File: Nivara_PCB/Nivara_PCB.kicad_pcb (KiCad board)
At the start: 2 copper layers, 102.2 x 83 mm, 40 parts, among them J1 NPN_IN, J10 PNP_OUT, J11 Analog_Out, J2 PNP_IN, J3 D_IN, J4 NPN_OUT, J5 RELAY, J6 RUN/STOP, J7 FUENTE, J8 RS485, J9 Analaog_In, Q1 IRLML6344, Q2 IRLML6344, U1 ESP32-S3-WROOM-1, U2 AP63203WU, U4 AP63205WU

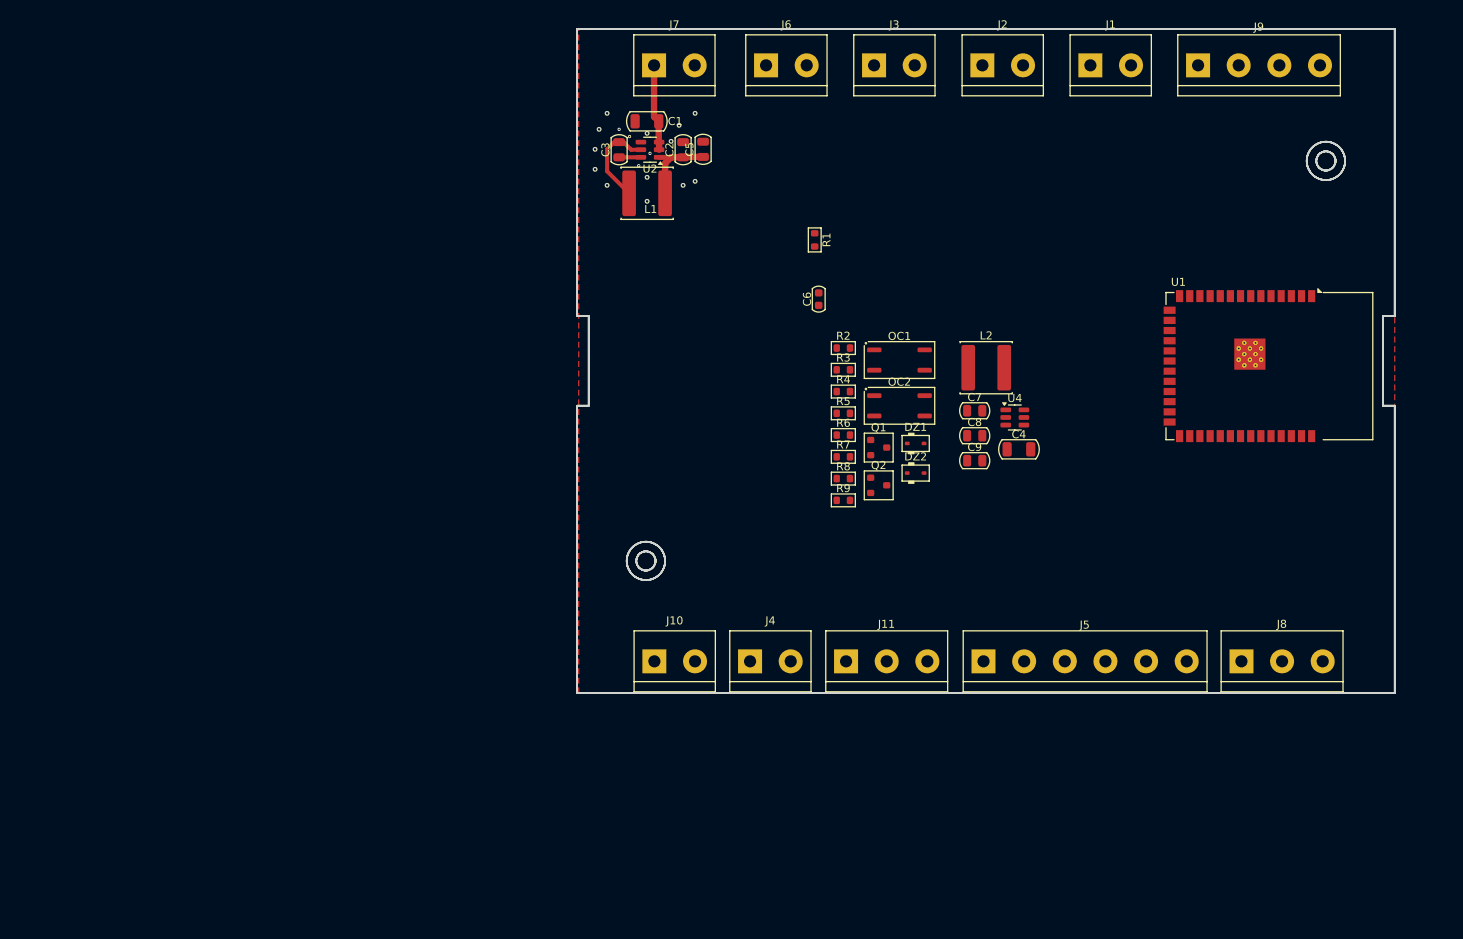
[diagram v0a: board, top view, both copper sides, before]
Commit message: Añadido de funciones NPN/PNP
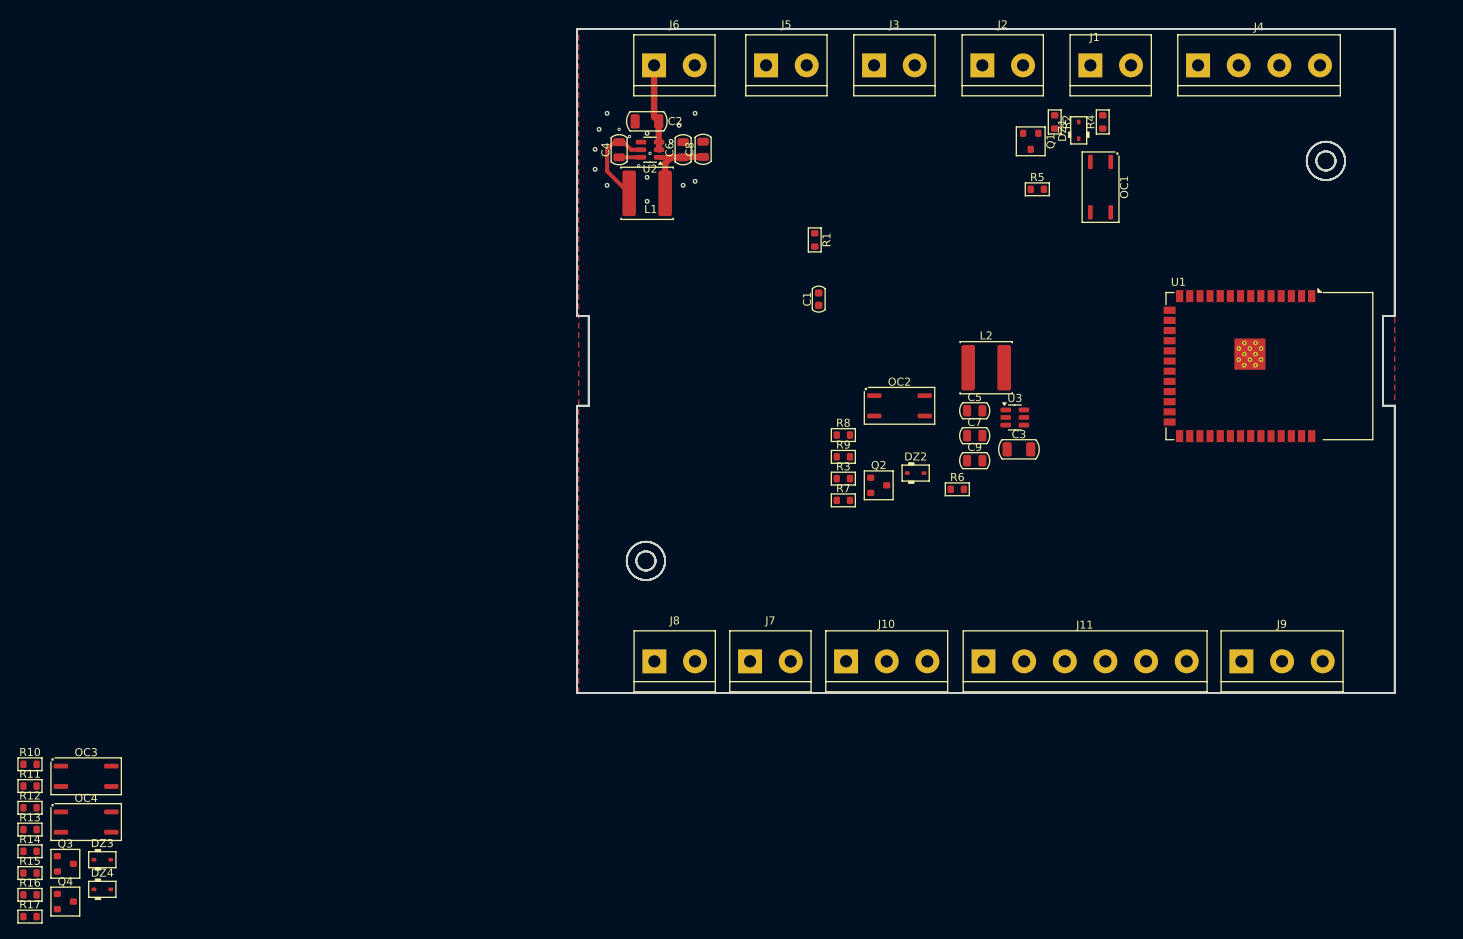
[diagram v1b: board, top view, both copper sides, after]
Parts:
- added DZ3: BZT52C10S, PCM_Diode_SMD_AKL:D_SOD-323, F.Cu at (39.0, 148.8)
- added DZ4: BZT52C10S, PCM_Diode_SMD_AKL:D_SOD-323, F.Cu at (39.0, 152.5)
- added OC3: LTV-356T, PCM_Package_SO_AKL:SO-4_4.4x3.9mm_P2.54mm, F.Cu at (36.9, 138.4)
- added OC4: LTV-356T, PCM_Package_SO_AKL:SO-4_4.4x3.9mm_P2.54mm, F.Cu at (36.9, 144.1)
- added Q3: IRLML6402, PCM_Package_TO_SOT_SMD_AKL:SOT-23, F.Cu at (34.3, 149.3)
- added Q4: IRLML6402, PCM_Package_TO_SOT_SMD_AKL:SOT-23, F.Cu at (34.3, 154.0)
- added R10: 7k, PCM_Resistor_SMD_AKL:R_0603_1608Metric, F.Cu at (29.9, 136.9)
- added R11: 22k, PCM_Resistor_SMD_AKL:R_0603_1608Metric, F.Cu at (29.9, 139.6)
- added R12: 1k, PCM_Resistor_SMD_AKL:R_0603_1608Metric, F.Cu at (29.9, 142.3)
- added R13: 10k, PCM_Resistor_SMD_AKL:R_0603_1608Metric, F.Cu at (29.9, 145.0)
- added R14: 7k, PCM_Resistor_SMD_AKL:R_0603_1608Metric, F.Cu at (29.9, 147.8)
- added R15: 22k, PCM_Resistor_SMD_AKL:R_0603_1608Metric, F.Cu at (29.9, 150.5)
- added R16: 1k, PCM_Resistor_SMD_AKL:R_0603_1608Metric, F.Cu at (29.9, 153.2)
- added R17: 10k, PCM_Resistor_SMD_AKL:R_0603_1608Metric, F.Cu at (29.9, 155.9)
- moved R4 46.8 mm to (164.0, 56.6), turned to 90 degrees
- moved DZ1 44.1 mm to (161.0, 57.6), turned to 90 degrees
- moved Q1 42.7 mm to (155.0, 59.0), turned to -90 degrees
- moved R2 38.7 mm to (158.0, 56.6), turned to -90 degrees
- moved R5 37.0 mm to (155.8, 65.0)
- moved OC1 33.1 mm to (163.7, 64.7), turned to -90 degrees
- moved R6 20.6 mm to (145.8, 102.5)
- renumbered C6 to C1, C1 to C2, C4 to C3, C3 to C4, C7 to C5, C2 to C6, C8 to C7, C5 to C8, J11 to J10, J5 to J11, J9 to J4, J6 to J5, J7 to J6, J4 to J7, J10 to J8, J8 to J9, R8 to R3, R3 to R6, R9 to R7, R6 to R8, R7 to R9, U4 to U3

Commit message: Cambios en pcb
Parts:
- moved R7 58.4 mm to (169.0, 59.0)
- moved Q2 58.4 mm to (172.0, 56.0)
- moved DZ2 52.4 mm to (168.0, 55.8), turned to 90 degrees
- moved R8 50.4 mm to (169.0, 62.0), turned to 90 degrees
- moved R6 50.3 mm to (165.0, 56.0), turned to -90 degrees
- moved R9 49.5 mm to (169.0, 66.0), turned to -90 degrees
- moved R3 48.0 mm to (156.0, 59.8), turned to -90 degrees
- moved OC2 45.0 mm to (173.0, 63.0), turned to -90 degrees
- moved R4 8.03 mm to (159.2, 63.0), turned to 0 degrees
- moved Q1 5.10 mm to (160.0, 60.0), turned to 0 degrees
- moved R5 3.50 mm to (159.2, 66.0)
- moved OC1 1.87 mm to (164.7, 63.1)
- moved DZ1 1.63 mm to (161.0, 56.0)
- moved R2 0.75 mm to (158.0, 55.8)

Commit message: Cambios en archivos a subir
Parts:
- added TP1: +VCC, TestPoint:TestPoint_Pad_1.0x1.0mm, F.Cu at (103.7, 55.1)
- added TP2: +3.3V, TestPoint:TestPoint_Pad_1.0x1.0mm, F.Cu at (105.9, 72.1)
- added TP3: +5V, TestPoint:TestPoint_Pad_1.0x1.0mm, F.Cu at (118.5, 58.4)
- added TP4: GND, TestPoint:TestPoint_Pad_1.0x1.0mm, F.Cu at (103.4, 51.7)
- moved C1 60.0 mm to (188.4, 75.2), turned to 180 degrees
- moved C3 59.1 mm to (109.9, 57.6)
- moved R1 56.5 mm to (184.4, 75.6), turned to 0 degrees
- moved U3 53.4 mm to (110.6, 61.1), turned to -90 degrees
- moved C9 53.1 mm to (113.5, 58.6), turned to 90 degrees
- moved C7 49.1 mm to (115.9, 58.6), turned to 90 degrees
- moved C5 42.3 mm to (112.9, 69.2)
- moved L2 40.9 mm to (116.0, 63.7)
- moved C8 8.31 mm to (108.2, 65.9), turned to -90 degrees
- moved C6 6.03 mm to (110.6, 66.0), turned to -90 degrees
- moved L1 3.76 mm to (103.8, 67.4)
- moved C2 3.28 mm to (104.9, 59.0)
- moved C4 2.43 mm to (102.1, 62.0)
- moved U2 2.43 mm to (106.0, 62.0)
- moved Q2 1.17 mm to (172.6, 57.0)
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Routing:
- net +5V: track 0.00 -> 26.5 mm
- net +3.3V: track 11.8 -> 26.7 mm
- net VCC: track 10.8 -> 23.5 mm
- net Net-(U3-SW): track 0.00 -> 10.8 mm
- net Net-(DZ2-K): track 0.00 -> 9.40 mm
- net Net-(DZ1-K): track 0.00 -> 8.39 mm
- net /NIVARA_BOARD/NPN_IN_1: track 0.00 -> 8.27 mm
- net /NIVARA_BOARD/NPN_IN/ESP_NPN_IN_1: track 0.00 -> 7.84 mm
- net /NIVARA_BOARD/NPN_IN_2: track 0.00 -> 7.65 mm
- net Net-(OC1-Pad1): track 0.00 -> 7.24 mm
- net Net-(U3-BST): track 0.00 -> 7.07 mm
- net /NIVARA_BOARD/NPN_IN/ESP_NPN_IN_2: track 0.00 -> 6.85 mm
- net Net-(OC2-Pad1): track 0.00 -> 5.84 mm
- net Net-(Q2-D): track 0.00 -> 4.55 mm
- net Net-(Q1-D): track 0.00 -> 2.46 mm
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- added copper zone on B.Cu, net GND

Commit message: Cambios en el diseño del pcb
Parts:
- moved R16 159.2 mm to (157.7, 58.3), turned to 180 degrees
- moved R15 158.8 mm to (157.2, 55.5), turned to -90 degrees
- moved R17 156.4 mm to (157.5, 65.4), turned to 90 degrees
- moved Q4 154.5 mm to (158.2, 61.6), turned to -90 degrees
- moved R14 153.7 mm to (152.8, 55.4), turned to -90 degrees
- moved DZ4 151.4 mm to (155.2, 55.5), turned to -90 degrees
- moved R10 144.5 mm to (149.3, 55.5), turned to -90 degrees
- moved OC4 142.5 mm to (153.5, 62.2), turned to -90 degrees
- moved DZ3 142.5 mm to (146.6, 55.5), turned to -90 degrees
- moved R11 141.8 mm to (144.0, 55.4), turned to -90 degrees
- moved R12 141.4 mm to (143.7, 58.4)
- moved Q3 139.9 mm to (143.5, 61.8)
- moved R13 139.1 mm to (143.8, 65.2)
- moved OC3 134.8 mm to (148.1, 62.1), turned to -90 degrees
- moved R5 10.4 mm to (169.2, 70.2), turned to -90 degrees
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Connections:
- R14 pad 1: /NIVARA_BOARD/PNP_IN_1 -> /NIVARA_BOARD/PNP_IN_2
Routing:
- net Net-(DZ3-K): track 0.00 -> 13.8 mm
- net Net-(DZ4-K): track 0.00 -> 12.3 mm
- net +3.3V: track 26.7 -> 16.5 mm
- net /NIVARA_BOARD/NPN_IN/ESP_NPN_IN_1: track 7.84 -> 0.00 mm
- net /NIVARA_BOARD/PNP_IN/ESP_PNP_IN_1: track 0.00 -> 6.69 mm
- net Net-(Q3-D): track 0.00 -> 6.05 mm
- net /NIVARA_BOARD/PNP_IN_2: track 0.00 -> 5.59 mm
- net /NIVARA_BOARD/PNP_IN_1: track 0.00 -> 5.29 mm
- net Net-(Q3-S): track 0.00 -> 5.19 mm
- net Net-(Q4-D): track 0.00 -> 5.18 mm
- net /NIVARA_BOARD/PNP_IN/ESP_PNP_IN_2: track 0.00 -> 3.05 mm
- net Net-(Q4-S): track 0.00 -> 2.42 mm
- net Net-(Q1-D): track 2.46 -> 4.35 mm
- net +5V: track 26.5 -> 24.7 mm
- net Net-(DZ1-K): track 8.39 -> 6.96 mm
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
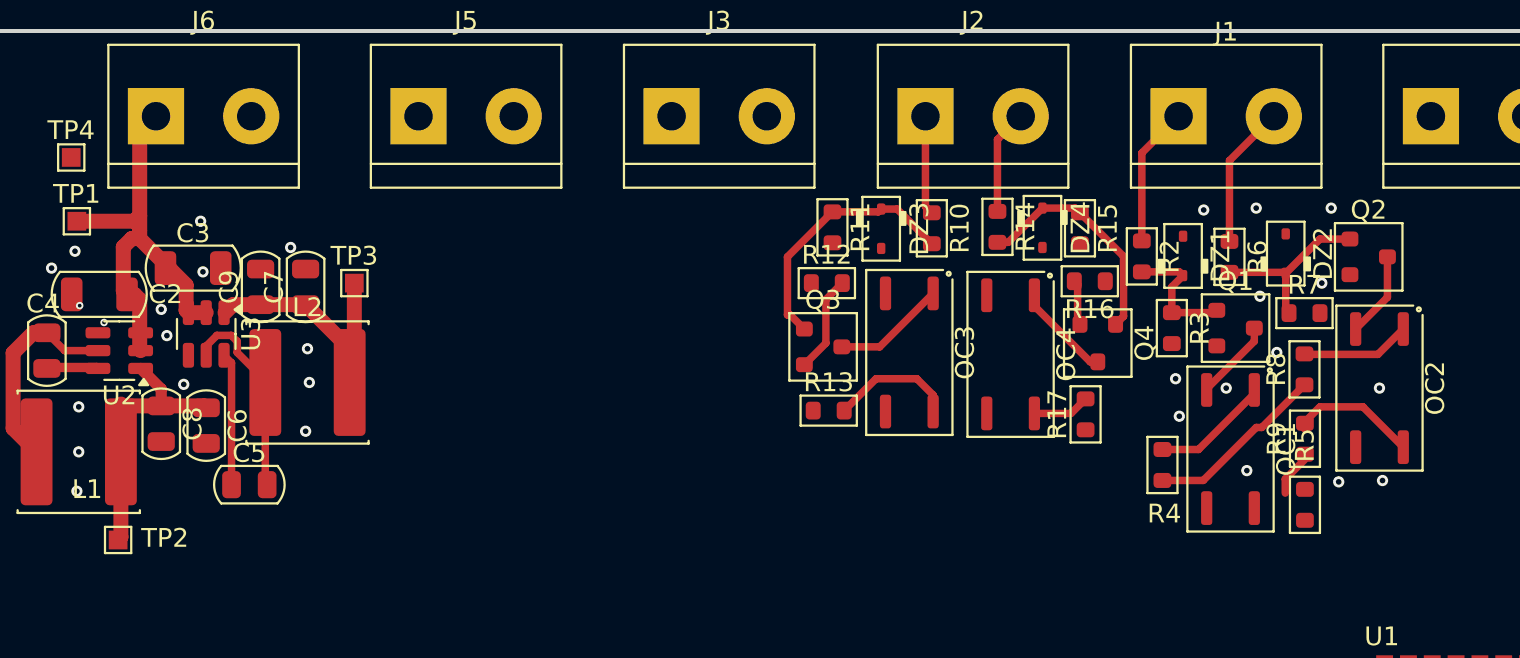
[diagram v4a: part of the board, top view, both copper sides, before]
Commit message: Modificación del PCB
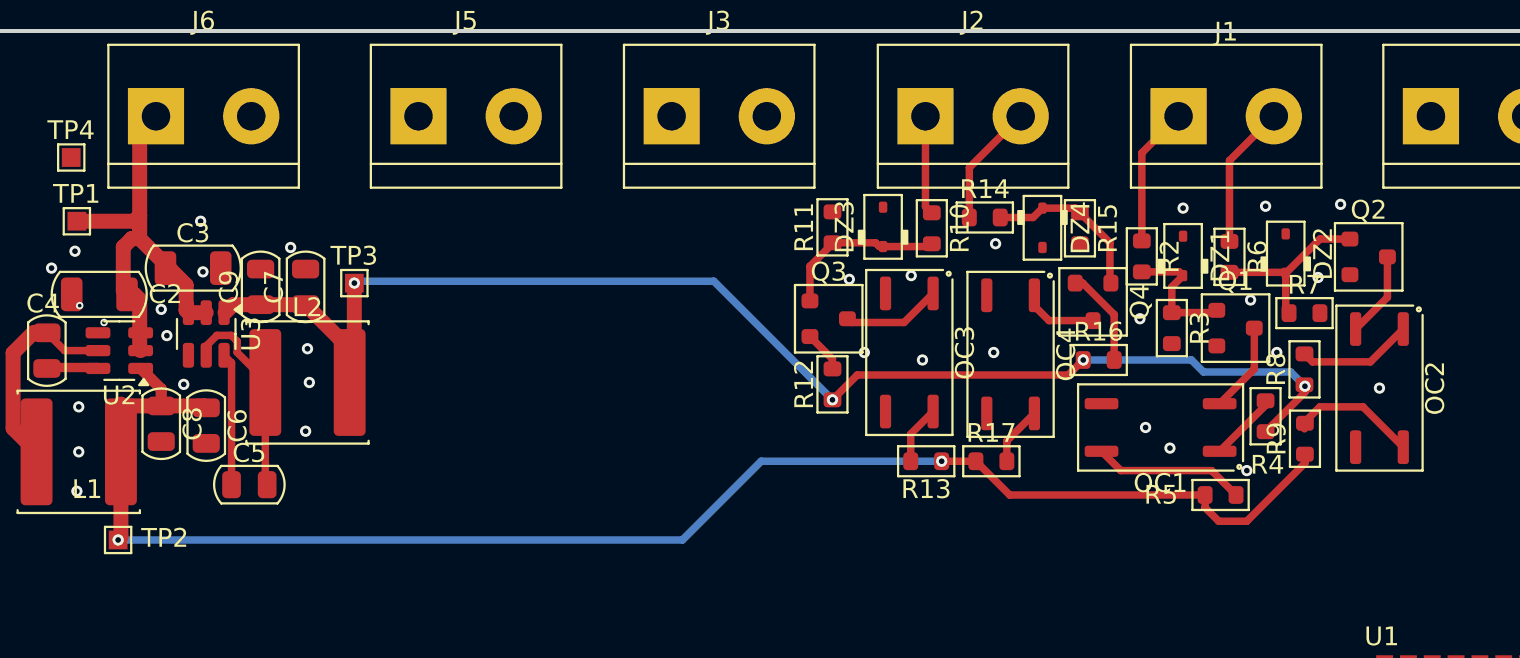
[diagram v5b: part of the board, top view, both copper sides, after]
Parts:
- moved R4 6.08 mm to (167.1, 65.5)
- moved R13 5.86 mm to (149.0, 67.9), turned to 180 degrees
- moved R17 5.61 mm to (152.5, 67.9), turned to 0 degrees
- moved R12 5.41 mm to (144.0, 63.8), turned to 90 degrees
- moved R5 4.53 mm to (164.7, 69.7), turned to 0 degrees
- moved R16 4.23 mm to (158.2, 62.5), turned to 0 degrees
- moved OC1 3.90 mm to (161.5, 66.1), turned to 180 degrees
- moved Q4 2.21 mm to (157.9, 59.4)
- moved Q3 1.53 mm to (143.8, 60.3)
- moved R14 0.84 mm to (152.1, 54.9), turned to 0 degrees
- moved DZ3 0.14 mm to (146.7, 55.4), turned to 90 degrees
- turned R11 to 90 degrees
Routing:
- net +3.3V: track 16.5 -> 82.8 mm, vias 0 -> 2
- net +5V: track 24.7 -> 73.1 mm, vias 0 -> 4
- net /NIVARA_BOARD/NPN_IN/ESP_NPN_IN_1: track 0.00 -> 8.14 mm
- net Net-(DZ3-K): track 13.8 -> 9.04 mm
- net /NIVARA_BOARD/PNP_IN/ESP_PNP_IN_1: track 6.69 -> 3.14 mm
- net Net-(DZ4-K): track 12.3 -> 8.99 mm
- net Net-(Q3-S): track 5.19 -> 2.22 mm
- net Net-(Q4-S): track 2.42 -> 5.19 mm
- net Net-(OC1-Pad1): track 6.33 -> 3.71 mm
- net Net-(Q4-D): track 5.18 -> 4.02 mm
- net /NIVARA_BOARD/PNP_IN_2: track 5.59 -> 6.53 mm
- net Net-(Q3-D): track 6.05 -> 5.29 mm
- net GND: vias 29 -> 33
